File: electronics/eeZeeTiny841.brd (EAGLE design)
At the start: 28.7 x 16.3 mm, 12 parts, among them IC1 ATtiny841, J2 avrisp, Q1 16MHz

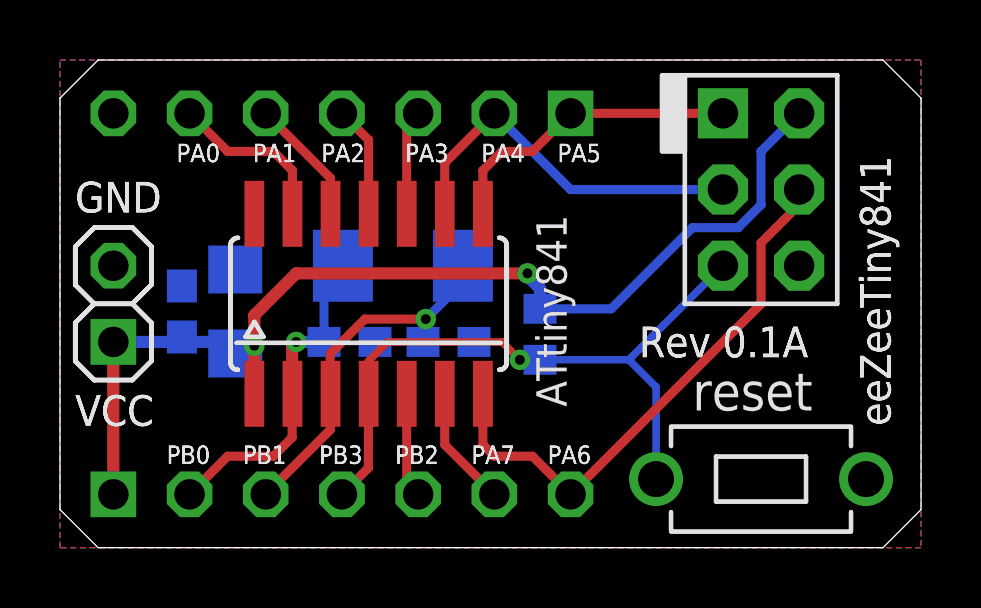
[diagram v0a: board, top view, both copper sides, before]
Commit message: revised layout, updated logo
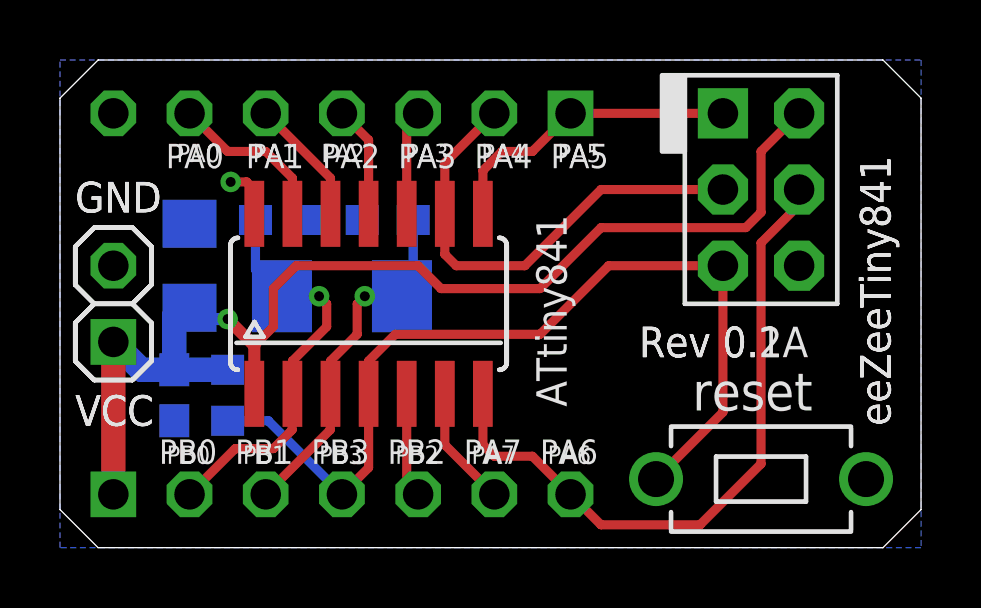
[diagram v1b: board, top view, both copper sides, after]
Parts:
- added U$1: BTLOGO-LOGO-MD, bt:BTLOGOM
- C1: value 0.1uF -> 104
- C2: value 100uF -> 106
- moved R1 10.6 mm to (5.59, 5.08)
- moved C5 4.66 mm to (7.37, 10.9)
- moved C4 4.54 mm to (10.9, 10.9), turned to 0 degrees
- moved C1 2.81 mm to (3.81, 5.08), turned to 270 degrees
- moved Q1 2.27 mm to (9.40, 8.38)
- moved C2 2.16 mm to (4.32, 9.40)
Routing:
- net !RESET: track 22.8 -> 30.8 mm, vias 1 -> 0
- net PA6: track 18.6 -> 22.6 mm
- net VCC: track 36.3 -> 39.9 mm, vias 2 -> 1
- net PA4: track 12.7 -> 15.9 mm
- net XTAL1: track 11.2 -> 13.5 mm
- net GND: track 0.00 -> 1.70 mm, vias 0 -> 1
- removed copper zone on layer 1, net GND
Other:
- board text added: "CC-BY-SA"
- board text added: "Rev 0.2"
